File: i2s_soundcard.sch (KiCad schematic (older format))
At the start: 2 parts

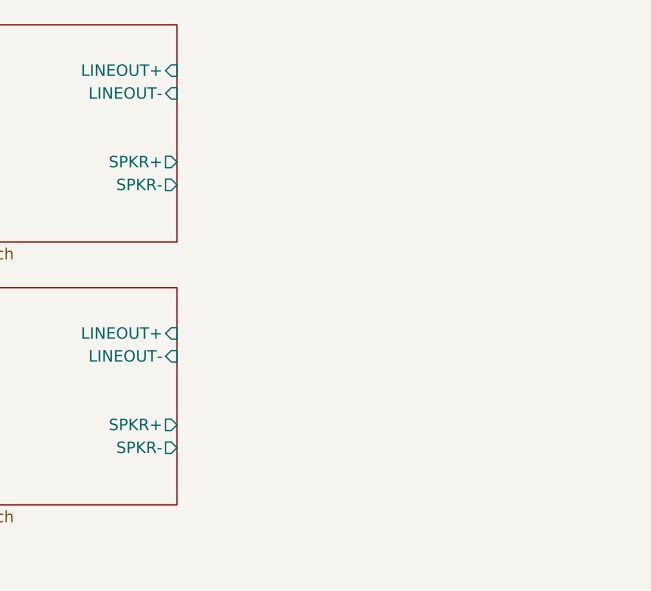
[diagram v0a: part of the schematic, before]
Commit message: schematic: Add speaker connector
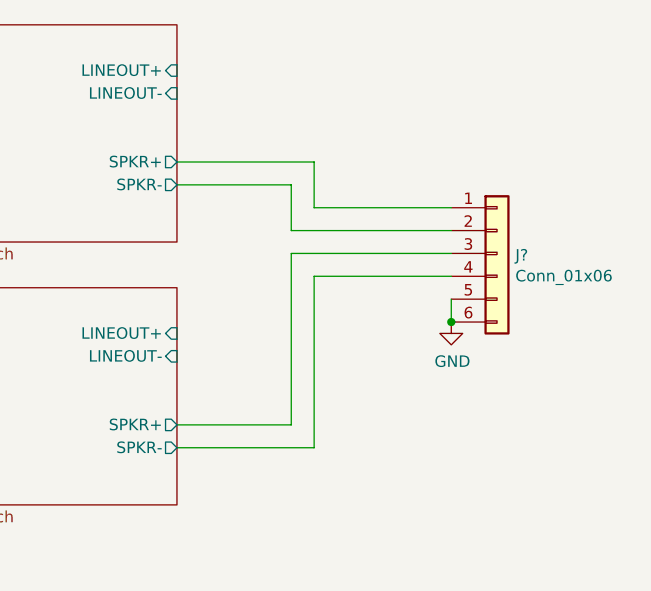
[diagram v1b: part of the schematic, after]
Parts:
- added J?: Conn_01x06, footprints:78171-0004, symbol Connector_Generic:Conn_01x06
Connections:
- net GND: now also J?.5 (Pin_5), J?.6 (Pin_6)
- net spkr_amp_left/SPKR+: now also J?.1 (Pin_1)
- net spkr_amp_left/SPKR-: now also J?.2 (Pin_2)
- net spkr_amp_right/SPKR+: now also J?.3 (Pin_3)
- net spkr_amp_right/SPKR-: now also J?.4 (Pin_4)
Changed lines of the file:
@@
 Wire Wire Line
 	7350 3250 7550 3250
+$Comp
+L Connector_Generic:Conn_01x06 J?
+U 1 1 6029263E
+P 10300 3700
+F 0 "J?" H 10380 3692 50  0000 L CNN
+F 1 "Conn_01x06" H 10380 3601 50  0000 L CNN
+F 2 "footprints:78171-0004" H 10300 3700 50  0001 C CNN
+F 3 "~" H 10300 3700 50  0001 C CNN
+	1    10300 3700
+	1    0    0    -1
+$EndComp
+$Comp
+L power:GND #PWR?
+U 1 1 60293F25
+P 10100 4000
+F 0 "#PWR?" H 10100 3750 50  0001 C CNN
+F 1 "GND" H 10105 3827 50  0000 C CNN
+F 2 "" H 10100 4000 50  0001 C CNN
+F 3 "" H 10100 4000 50  0001 C CNN
+	1    10100 4000
+	1    0    0    -1
+$EndComp
+Wire Wire Line
+	10100 4000 10100 3900
+Connection ~ 10100 4000
+Wire Wire Line
+	10100 3800 9500 3800
+Wire Wire Line
+	9500 3800 9500 4550
+Wire Wire Line
+	9500 4550 8900 4550
+Wire Wire Line
+	8900 4450 9400 4450
+Wire Wire Line
+	9400 4450 9400 3700
+Wire Wire Line
+	9400 3700 10100 3700
+Wire Wire Line
+	10100 3600 9400 3600
+Wire Wire Line
+	9400 3600 9400 3400
+Wire Wire Line
+	9400 3400 8900 3400
+Wire Wire Line
+	10100 3500 9500 3500
+Wire Wire Line
+	9500 3500 9500 3300
+Wire Wire Line
+	9500 3300 8900 3300
 $EndSCHEMATC

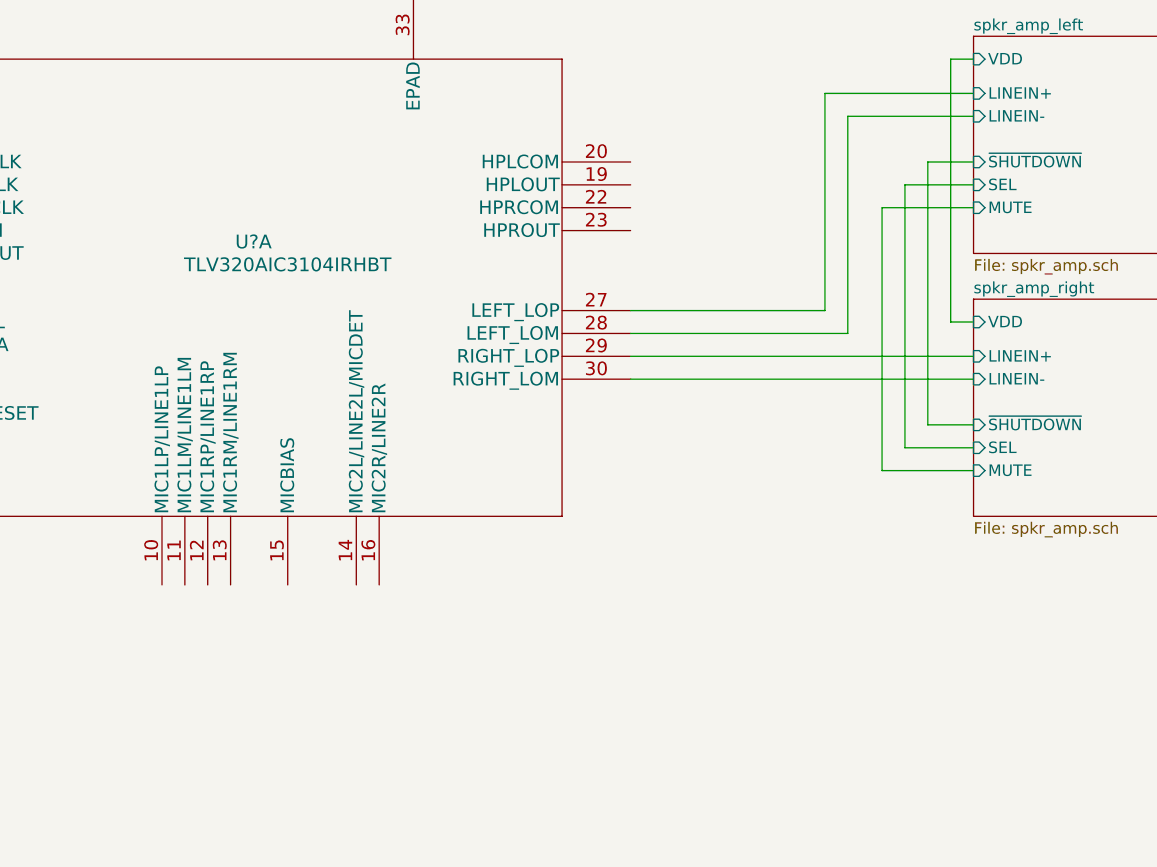
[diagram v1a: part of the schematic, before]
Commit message: schematic: wire up most of the headphone jack
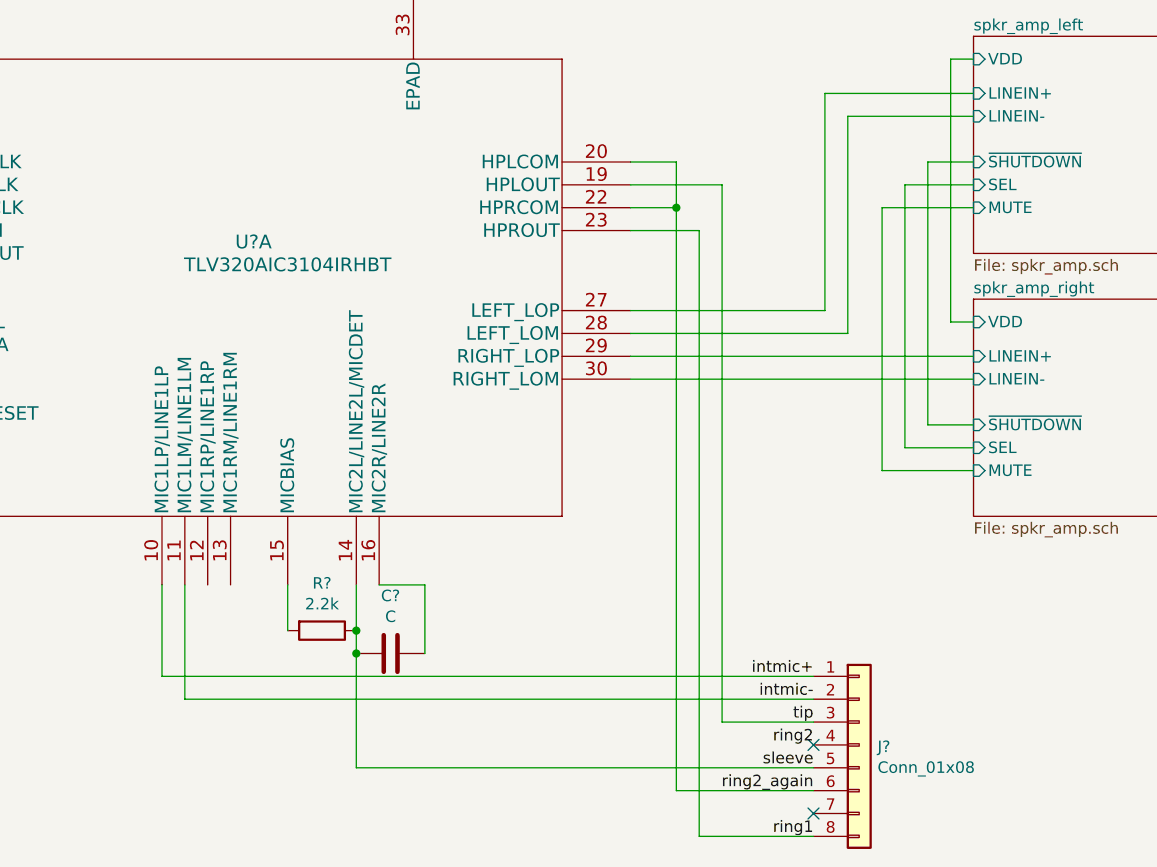
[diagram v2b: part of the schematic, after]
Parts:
- added C?: C, symbol Device:C
- added J?: Conn_01x08, footprints:FF18-8A-R11AD-B-3H, symbol Connector_Generic:Conn_01x08
- added R?: 2.2k, symbol Device:R
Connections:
- net intmic+: now reaches U?.10 (MIC1LP/LINE1LP)
- net intmic+: now also J?.1 (Pin_1)
- net intmic-: now reaches U?.11 (MIC1LM/LINE1LM)
- net intmic-: now also J?.2 (Pin_2)
- net sleeve: now reaches U?.14 (MIC2L/LINE2L/MICDET)
- net sleeve: now also C?.2, J?.5 (Pin_5), R?.1
- net at U?.15 (MICBIAS): now also R?.2
- net at U?.16 (MIC2R/LINE2R): now also C?.1
- net tip: now reaches U?.19 (HPLOUT)
- net tip: now also J?.3 (Pin_3)
- net ring2_again: now reaches U?.20 (HPLCOM)
- net ring2_again: now also U?.22 (HPRCOM), J?.6 (Pin_6)
- net ring1: now reaches U?.23 (HPROUT)
- net ring1: now also J?.8 (Pin_8)
- new net ring2: J?.4 (Pin_4)
- no-connect marks 0 -> 2
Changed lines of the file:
@@
 Wire Wire Line
 	9500 3300 8900 3300
+$Comp
+L Connector_Generic:Conn_01x08 J?
+U 1 1 60262BE3
+P 7050 5800
+F 0 "J?" H 7130 5792 50  0000 L CNN
+F 1 "Conn_01x08" H 7130 5701 50  0000 L CNN
+F 2 "footprints:FF18-8A-R11AD-B-3H" H 7050 5800 50  0001 C CNN
+F 3 "~" H 7050 5800 50  0001 C CNN
+	1    7050 5800
+	1    0    0    -1
+$EndComp
+Text Label 6850 5500 2    50   ~ 0
+intmic+
+Text Label 6850 5600 2    50   ~ 0
+intmic-
+Text Label 6850 5700 2    50   ~ 0
+tip
+Text Label 6850 5800 2    50   ~ 0
+ring2
+Text Label 6850 5900 2    50   ~ 0
+sleeve
+Text Label 6850 6000 2    50   ~ 0
+ring2_again
+Text Label 6850 6200 2    50   ~ 0
+ring1
+Wire Wire Line
+	4000 5500 4000 5100
+Wire Wire Line
+	4100 5600 4100 5100
+Wire Wire Line
+	4000 5500 6850 5500
+Wire Wire Line
+	4100 5600 6850 5600
+Wire Wire Line
+	6850 5700 6450 5700
+Wire Wire Line
+	6450 5700 6450 3350
+Wire Wire Line
+	6450 3350 6050 3350
+Wire Wire Line
+	6050 3550 6350 3550
+Wire Wire Line
+	6350 3550 6350 6200
+Wire Wire Line
+	6350 6200 6850 6200
+Wire Wire Line
+	6850 6000 6250 6000
+Wire Wire Line
+	6250 6000 6250 3450
+Wire Wire Line
+	6250 3450 6050 3450
+Wire Wire Line
+	6250 3450 6250 3250
+Wire Wire Line
+	6250 3250 6050 3250
+Connection ~ 6250 3450
+$Comp
+L Device:R R?
+U 1 1 60271543
+P 4700 5300
+F 0 "R?" V 4493 5300 50  0000 C CNN
+F 1 "2.2k" V 4584 5300 50  0000 C CNN
+F 2 "" V 4630 5300 50  0001 C CNN
+F 3 "~" H 4700 5300 50  0001 C CNN
+	1    4700 5300
+	0    1    1    0
+$EndComp
+Connection ~ 4850 5300
+Wire Wire Line
+	4850 5300 4850 5100
+$Comp
+L Device:C C?
+U 1 1 60271C8D
+P 5000 5400
+F 0 "C?" V 4748 5400 50  0000 C CNN
+F 1 "C" V 4839 5400 50  0000 C CNN
+F 2 "" H 5038 5250 50  0001 C CNN
+F 3 "~" H 5000 5400 50  0001 C CNN
+	1    5000 5400
+	0    1    1    0
+$EndComp
+Connection ~ 4850 5400
+Wire Wire Line
+	4850 5400 4850 5300
+Wire Wire Line
+	5150 5400 5150 5100
+Wire Wire Line
+	5150 5100 4950 5100
+Wire Wire Line
+	4550 5300 4550 5100
+Wire Wire Line
+	4850 5900 6850 5900
+Wire Wire Line
+	4850 5400 4850 5900
+NoConn ~ 6850 5800
+NoConn ~ 6850 6100
 $EndSCHEMATC

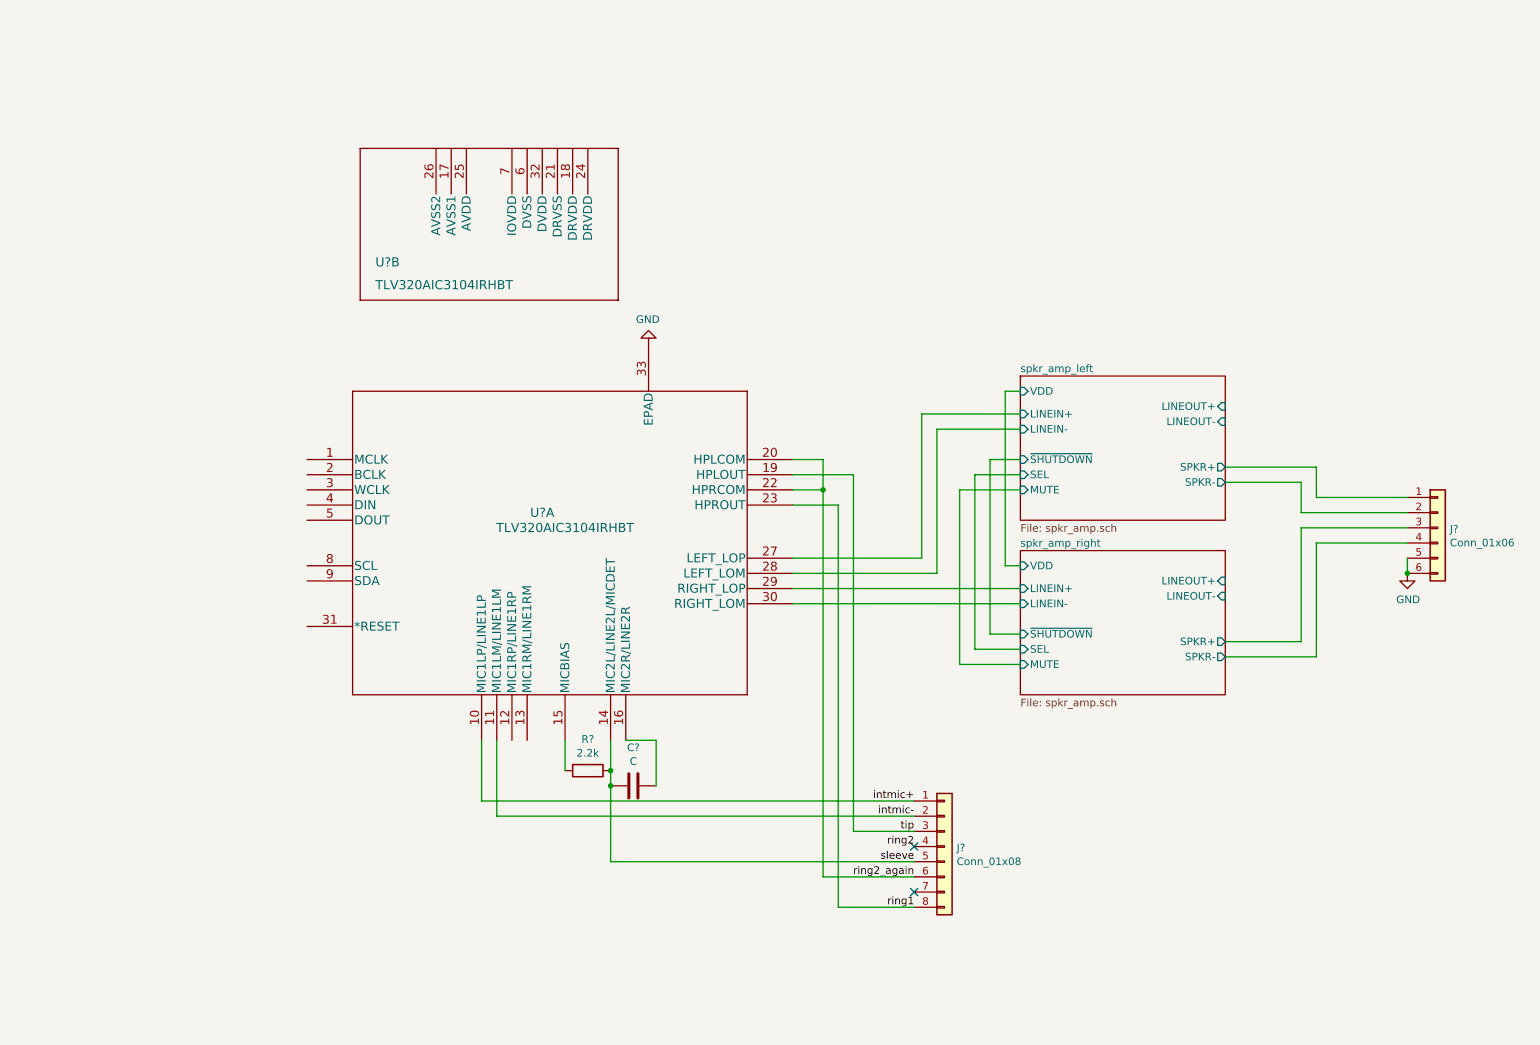
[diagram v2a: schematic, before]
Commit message: Import FSA2275 footprint from SnapEDA; annotate symbols.
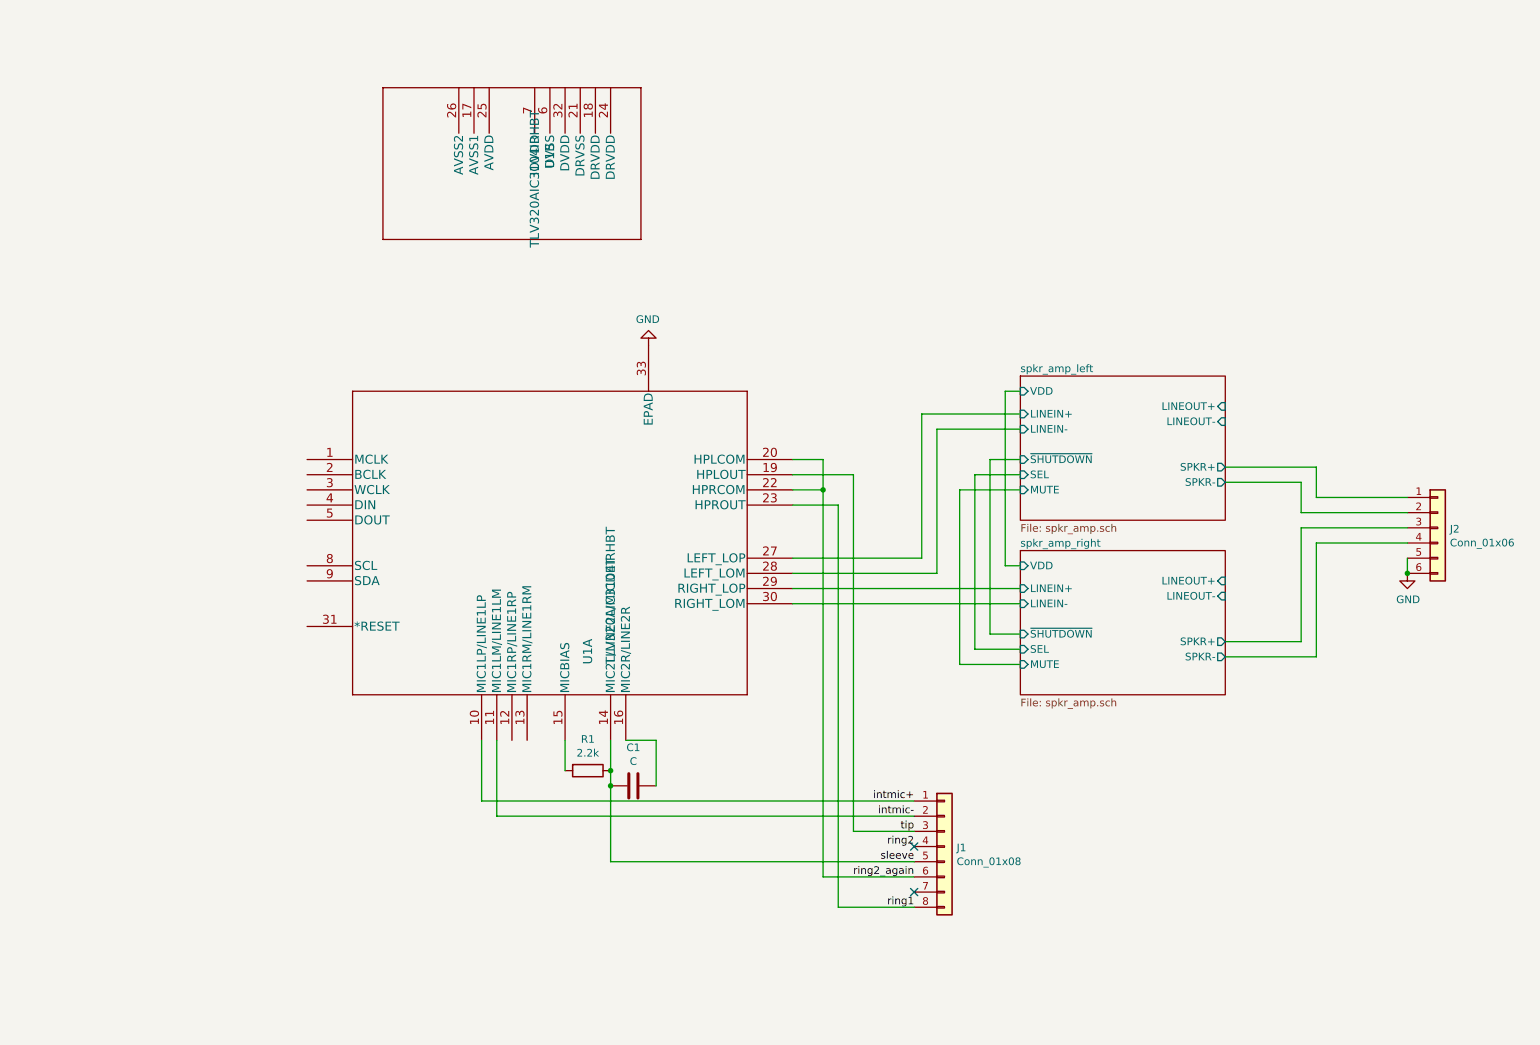
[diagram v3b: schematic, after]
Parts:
- C1: renamed from C?; footprint (none) -> Capacitor_SMD:C_0402_1005Metric
- R1: renamed from R?; footprint (none) -> Resistor_SMD:R_0402_1005Metric
- U1: renamed from U?; footprint RHB32_3P45X3P45 -> footprints:TLV320AIC3104IRHBT
- gave numbers to parts that had none: 2
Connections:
- net GND: now also U1.33 (EPAD); no longer U1.33 (EPAD)
- net intmic+: now also U1.10 (MIC1LP/LINE1LP); no longer U1.10 (MIC1LP/LINE1LP)
- net intmic-: now also U1.11 (MIC1LM/LINE1LM); no longer U1.11 (MIC1LM/LINE1LM)
- net ring1: now also U1.23 (HPROUT); no longer U1.23 (HPROUT)
- net ring2_again: now also U1.20 (HPLCOM), U1.22 (HPRCOM); no longer U1.20 (HPLCOM), U1.22 (HPRCOM)
- net sleeve: now also U1.14 (MIC2L/LINE2L/MICDET); no longer U1.14 (MIC2L/LINE2L/MICDET)
- net spkr_amp_left/LINEIN+: now also U1.27 (LEFT_LOP); no longer U1.27 (LEFT_LOP)
- net spkr_amp_left/LINEIN-: now also U1.28 (LEFT_LOM); no longer U1.28 (LEFT_LOM)
- net spkr_amp_right/LINEIN+: now also U1.29 (RIGHT_LOP); no longer U1.29 (RIGHT_LOP)
- net spkr_amp_right/LINEIN-: now also U1.30 (RIGHT_LOM); no longer U1.30 (RIGHT_LOM)
- net tip: now also U1.19 (HPLOUT); no longer U1.19 (HPLOUT)
- net at R1.2: now also U1.15 (MICBIAS); no longer U1.15 (MICBIAS)
- net at C1.1: now also U1.16 (MIC2R/LINE2R); no longer U1.16 (MIC2R/LINE2R)
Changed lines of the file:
@@
 $EndDescr
 $Comp
-L TLV320AIC3104IRHBT:TLV320AIC3104IRHBT U?
-U 1 1 602615AE
+L TLV320AIC3104IRHBT:TLV320AIC3104IRHBT U1
+U 2 1 602615AE
+P 4200 1300
+F 0 "U1" H 4150 1550 60  0000 C CNN
+F 1 "TLV320AIC3104IRHBT" H 4300 1450 60  0000 C CNN
+F 2 "footprints:TLV320AIC3104IRHBT" H 5800 1540 60  0001 C CNN
+F 3 "" H 4200 1300 60  0000 C CNN
+	2    4200 1300
+	0    1    1    0
+$EndComp
+$Comp
+L TLV320AIC3104IRHBT:TLV320AIC3104IRHBT U1
+U 1 1 602651EC
 P 4450 3850
-F 0 "U?" H 4400 4100 60  0000 C CNN
-F 1 "TLV320AIC3104IRHBT" H 4550 4000 60  0000 C CNN
-F 2 "RHB32_3P45X3P45" H 6050 4090 60  0001 C CNN
+F 0 "U1" V 4700 3100 60  0000 L CNN
+F 1 "TLV320AIC3104IRHBT" V 4850 3100 60  0000 L CNN
+F 2 "footprints:TLV320AIC3104IRHBT" H 6050 4090 60  0001 C CNN
 F 3 "" H 4450 3850 60  0000 C CNN
 	1    4450 3850
 	1    0    0    -1
-$EndComp
-$Comp
-L TLV320AIC3104IRHBT:TLV320AIC3104IRHBT U?
-U 2 1 602651EC
-P 4050 1700
-F 0 "U?" V 4300 950 60  0000 L CNN
-F 1 "TLV320AIC3104IRHBT" V 4450 950 60  0000 L CNN
-F 2 "RHB32_3P45X3P45" H 5650 1940 60  0001 C CNN
-F 3 "" H 4050 1700 60  0000 C CNN
-	2    4050 1700
-	0    1    1    0
 $EndComp
 $Sheet
@@
 	6050 4200 7550 4200
 $Comp
-L power:GND #PWR?
+L power:GND #PWR01
 U 1 1 6028DD6A
 P 5100 2500
-F 0 "#PWR?" H 5100 2250 50  0001 C CNN
+F 0 "#PWR01" H 5100 2250 50  0001 C CNN
 F 1 "GND" H 5105 2327 50  0000 C CNN
 F 2 "" H 5100 2500 50  0001 C CNN
@@
 	7350 3250 7550 3250
 $Comp
-L Connector_Generic:Conn_01x06 J?
+L Connector_Generic:Conn_01x06 J2
 U 1 1 6029263E
 P 10300 3700
-F 0 "J?" H 10380 3692 50  0000 L CNN
+F 0 "J2" H 10380 3692 50  0000 L CNN
 F 1 "Conn_01x06" H 10380 3601 50  0000 L CNN
 F 2 "footprints:78171-0004" H 10300 3700 50  0001 C CNN
@@
 $EndComp
 $Comp
-L power:GND #PWR?
+L power:GND #PWR02
 U 1 1 60293F25
 P 10100 4000
-F 0 "#PWR?" H 10100 3750 50  0001 C CNN
+F 0 "#PWR02" H 10100 3750 50  0001 C CNN
 F 1 "GND" H 10105 3827 50  0000 C CNN
 F 2 "" H 10100 4000 50  0001 C CNN
@@
 	9500 3300 8900 3300
 $Comp
-L Connector_Generic:Conn_01x08 J?
+L Connector_Generic:Conn_01x08 J1
 U 1 1 60262BE3
 P 7050 5800
-F 0 "J?" H 7130 5792 50  0000 L CNN
+F 0 "J1" H 7130 5792 50  0000 L CNN
 F 1 "Conn_01x08" H 7130 5701 50  0000 L CNN
 F 2 "footprints:FF18-8A-R11AD-B-3H" H 7050 5800 50  0001 C CNN
@@
 Connection ~ 6250 3450
 $Comp
-L Device:R R?
+L Device:R R1
 U 1 1 60271543
 P 4700 5300
-F 0 "R?" V 4493 5300 50  0000 C CNN
+F 0 "R1" V 4493 5300 50  0000 C CNN
 F 1 "2.2k" V 4584 5300 50  0000 C CNN
-F 2 "" V 4630 5300 50  0001 C CNN
+F 2 "Resistor_SMD:R_0402_1005Metric" V 4630 5300 50  0001 C CNN
 F 3 "~" H 4700 5300 50  0001 C CNN
 	1    4700 5300
@@
 	4850 5300 4850 5100
 $Comp
-L Device:C C?
+L Device:C C1
 U 1 1 60271C8D
 P 5000 5400
-F 0 "C?" V 4748 5400 50  0000 C CNN
+F 0 "C1" V 4748 5400 50  0000 C CNN
 F 1 "C" V 4839 5400 50  0000 C CNN
-F 2 "" H 5038 5250 50  0001 C CNN
+F 2 "Capacitor_SMD:C_0402_1005Metric" H 5038 5250 50  0001 C CNN
 F 3 "~" H 5000 5400 50  0001 C CNN
 	1    5000 5400
